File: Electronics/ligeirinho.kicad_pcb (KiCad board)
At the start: 2 copper layers, 76.5 x 56 mm, 30 parts, among them J1 Bateria, J10 ponte H ld ESP, J11 VS1838B, J12 MPU6050, J13 ADNS-9500, J14 ADNS-9500 3V3, J2 ESP32 esq, J3 ESP32 dir, J4 VL53L0X 1, J5 VL53L0X 2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

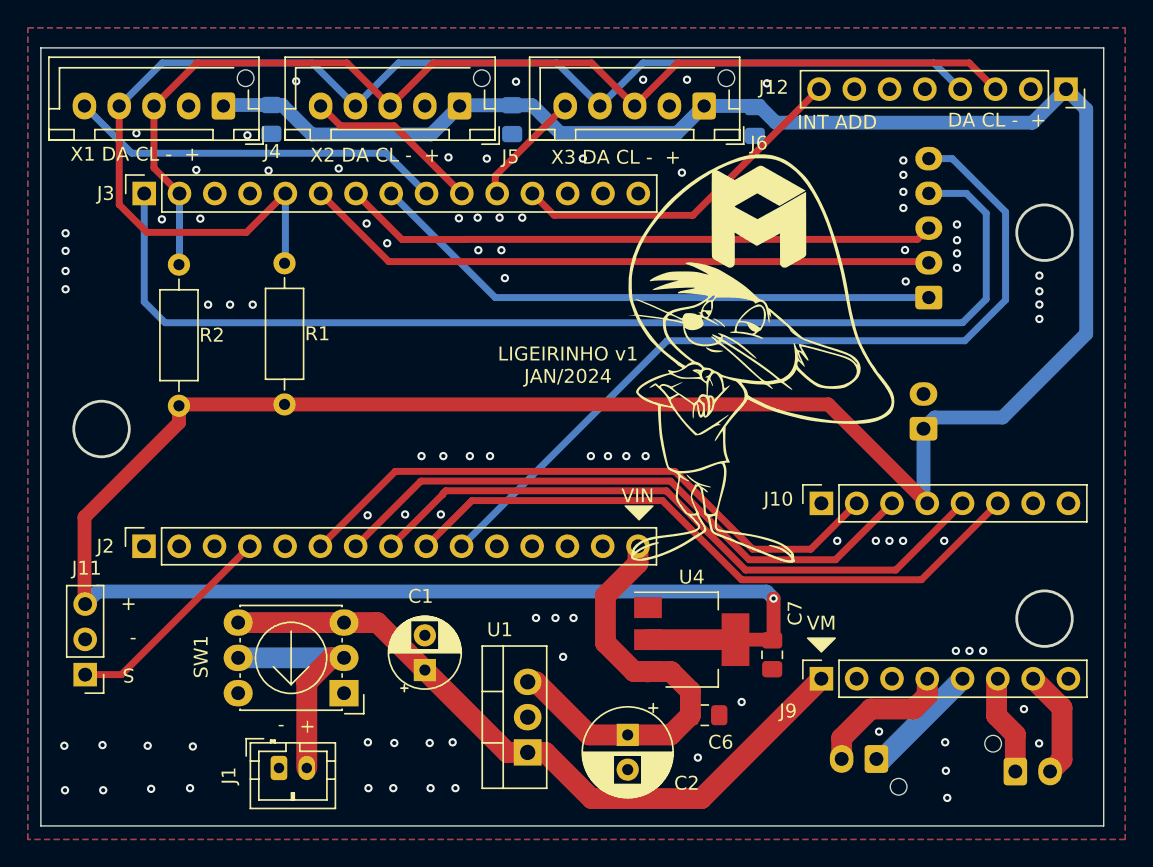
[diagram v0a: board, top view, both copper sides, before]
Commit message: fix: change pcb size from 76mm to 77mm
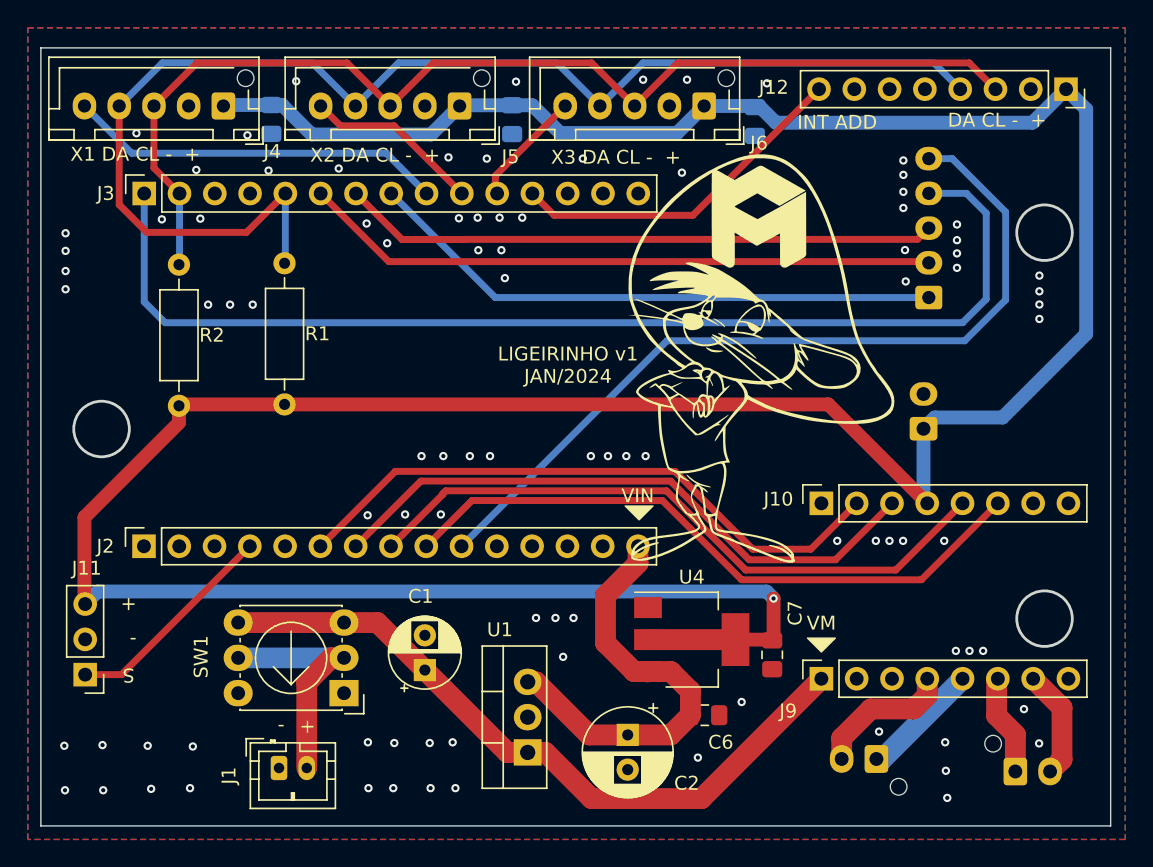
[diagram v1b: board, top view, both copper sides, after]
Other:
- board size 76.5 x 56 mm -> 77 x 56 mm
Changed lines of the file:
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@@
     )
     (stroke (width 0.1) (type solid)) (fill solid) (layer "F.SilkS"))
-  (gr_line (start 176.5 156) (end 100 156)
+  (gr_line (start 177 156) (end 100 156)
     (stroke (width 0.1) (type default)) (layer "Edge.Cuts"))
-  (gr_line (start 100 100) (end 176.5 100)
+  (gr_line (start 100 100) (end 177 100)
     (stroke (width 0.1) (type default)) (layer "Edge.Cuts"))
   (gr_circle (center 104.37 127.43) (end 106.37 127.43)
     (stroke (width 0.2) (type default)) (fill none) (layer "Edge.Cuts"))
-  (gr_line (start 176.5 100) (end 176.5 156)
+  (gr_line (start 177 100) (end 177 156)
     (stroke (width 0.1) (type default)) (layer "Edge.Cuts"))
   (gr_circle (center 172.24 113.3) (end 174.24 113.3)
@@
   )
   (dimension (type aligned) (layer "Dwgs.User")
-    (pts (xy 100 100) (xy 176.5 100))
-    (height -4.242)
-    (gr_text "76,5 mm" (at 138.25 94.608) (layer "Dwgs.User")
-      (effects (font (size 1 1) (thickness 0.15)))
-    )
-    (format (prefix "") (suffix "") (units 3) (units_format 1) (precision 4) suppress_zeroes)
-    (style (thickness 0.1) (arrow_length 1.27) (text_position_mode 0) (extension_height 0.58642) (extension_offset 0.5) keep_text_aligned)
-  )
-  (dimension (type aligned) (layer "Dwgs.User")
     (pts (xy 172.24 113.3) (xy 172.24 100.076))
     (height 9.37)
@@
     (height -11.402)
     (gr_text "14,876 mm" (at 182.492 148.518 90) (layer "Dwgs.User")
+      (effects (font (size 1 1) (thickness 0.15)))
+    )
+    (format (prefix "") (suffix "") (units 3) (units_format 1) (precision 4) suppress_zeroes)
+    (style (thickness 0.1) (arrow_length 1.27) (text_position_mode 0) (extension_height 0.58642) (extension_offset 0.5) keep_text_aligned)
+  )
+  (dimension (type aligned) (layer "Dwgs.User")
+    (pts (xy 100 100) (xy 177 100))
+    (height -3.734)
+    (gr_text "77 mm" (at 138.5 95.116) (layer "Dwgs.User")
       (effects (font (size 1 1) (thickness 0.15)))
     )
@@
         (xy 178.054 156.972)
         (xy 99.06 156.972)
-        (xy 99.06 156.972)
       )

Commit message: feat: add autonomous stategy
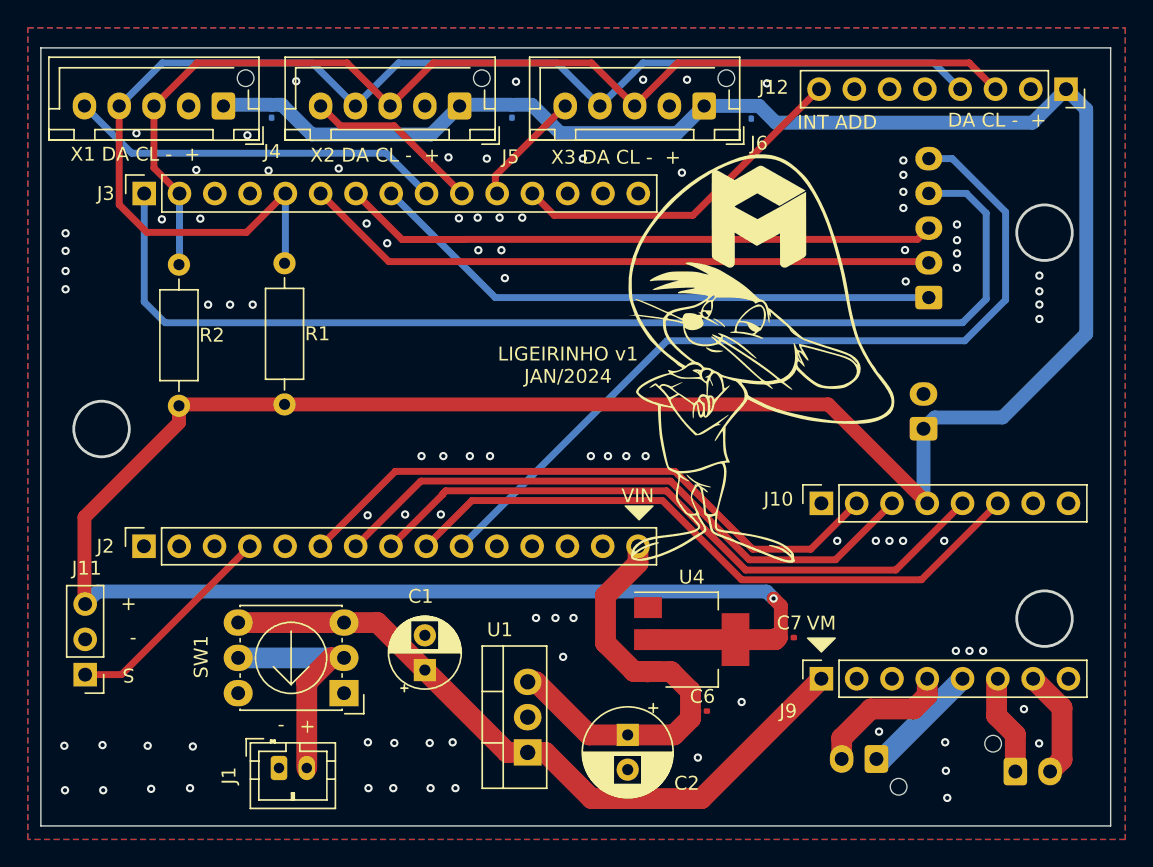
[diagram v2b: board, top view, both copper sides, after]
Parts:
- C3, C4, C5, C6, C7: footprint Capacitor_SMD:C_0805_2012Metric_Pad1.18x1.45mm_HandSolder -> Capacitor_SMD:C_0201_0603Metric
- moved C7 1.75 mm to (153.9, 142.4), turned to 0 degrees
- moved C5 0.59 mm to (151.1, 104.8)
- moved C4 0.46 mm to (133.9, 104.7)
- moved C3 0.44 mm to (116.6, 104.7)
- moved C6 0.34 mm to (147.6, 147.7)
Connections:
- SW1 pad 1: (no net) -> Net-(J1-Pin_2)
- SW1 pad 4: 2s -> (no net)
- SW1 pad C: Net-(J1-Pin_2) -> (no net)
